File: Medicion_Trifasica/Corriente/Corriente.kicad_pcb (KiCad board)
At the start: 4 copper layers, 49 x 25 mm, 13 parts, among them IC1 AMS1117-3.3, J1 XADC_Input, J2 Screw_Terminal_01x02, J3 XADC_Ref, J4 XADC_Input, U1 ACS725xLCTR-20AB, U2 LM358

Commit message: PCB de la medicion de corriente
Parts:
- moved C3 76.8 mm to (155.4, 97.2)
- moved J1 76.8 mm to (167.8, 103.0)
- moved J2 76.8 mm to (129.5, 103.4)
- moved J3 76.8 mm to (167.8, 99.4)
- moved J4 76.8 mm to (151.9, 89.3)
- moved R1 76.8 mm to (145.4, 105.3)
- moved R2 76.8 mm to (146.4, 108.3)
- moved R3 76.8 mm to (160.3, 95.7)
- moved U1 76.8 mm to (137.4, 105.9)
- moved U2 76.8 mm to (152.8, 104.6)
- moved C1 76.8 mm to (141.7, 107.4)
- moved IC1 76.8 mm to (149.4, 96.1)
- moved R4 76.8 mm to (163.7, 96.6)

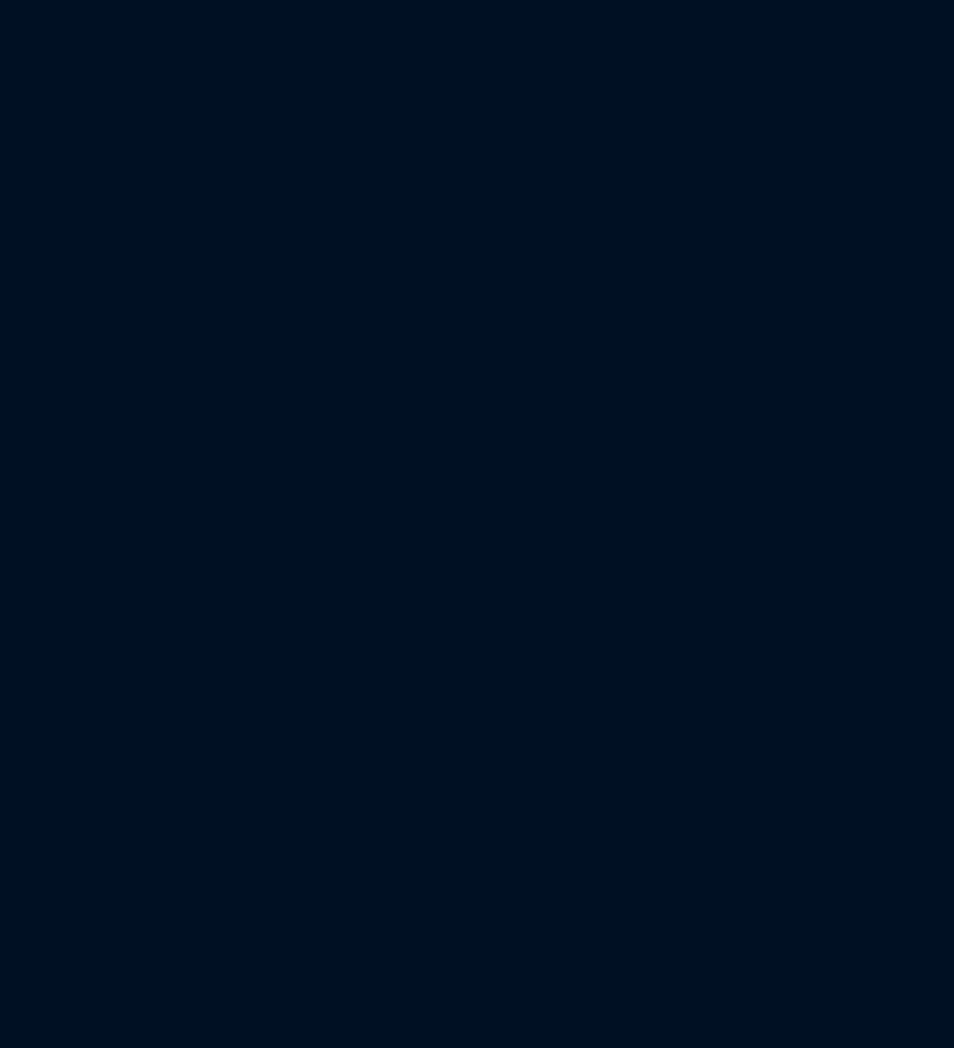
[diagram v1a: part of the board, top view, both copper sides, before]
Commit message: Correciones PCBs
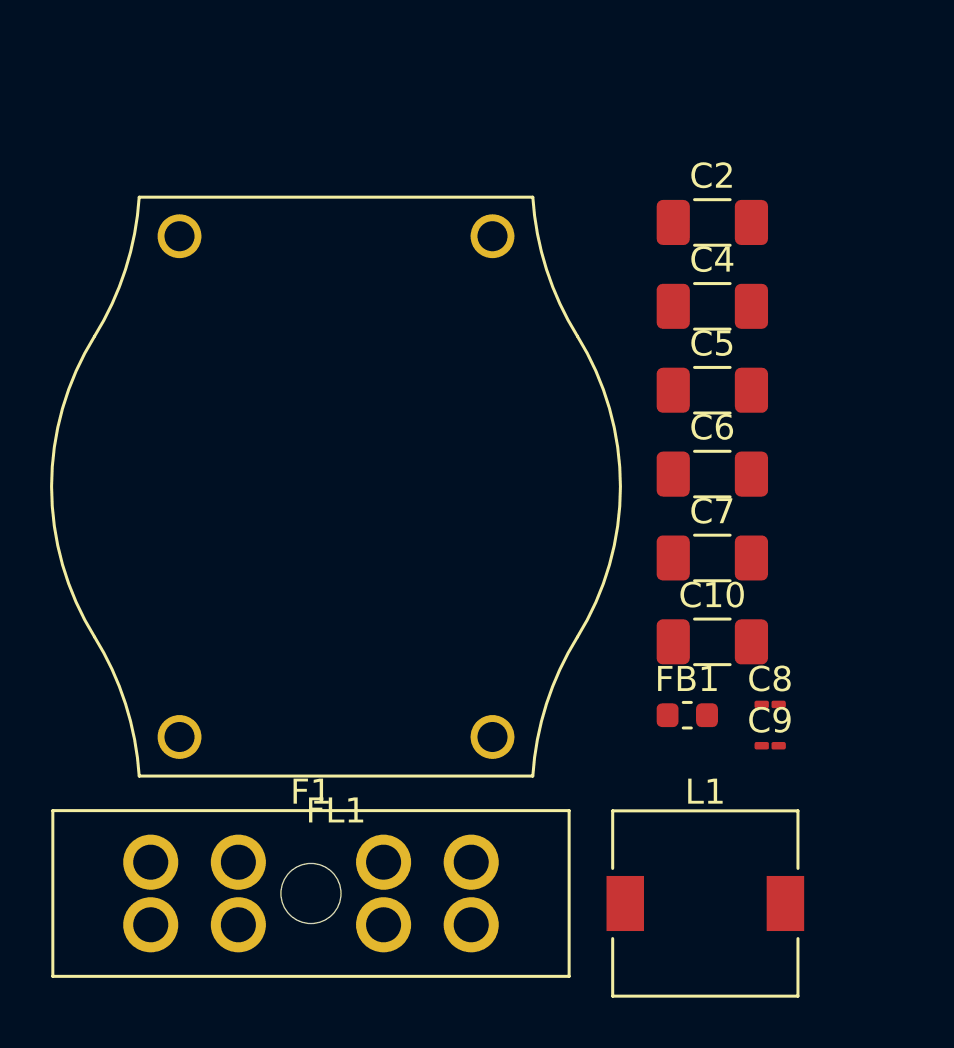
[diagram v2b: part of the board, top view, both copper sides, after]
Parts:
- added C10: 100 nF, Capacitor_SMD:C_1206_3216Metric_Pad1.33x1.80mm_HandSolder, F.Cu at (105.0, 115.7)
- added C2: 0.1 uF, Capacitor_SMD:C_1206_3216Metric_Pad1.33x1.80mm_HandSolder, F.Cu at (105.0, 98.9)
- added C4: 470 uF, Capacitor_SMD:C_1206_3216Metric_Pad1.33x1.80mm_HandSolder, F.Cu at (105.0, 102.2)
- added C5: 100 nF, Capacitor_SMD:C_1206_3216Metric_Pad1.33x1.80mm_HandSolder, F.Cu at (105.0, 105.6)
- added C6: 100 nF, Capacitor_SMD:C_1206_3216Metric_Pad1.33x1.80mm_HandSolder, F.Cu at (105.0, 109.0)
- added C7: 100 nF, Capacitor_SMD:C_1206_3216Metric_Pad1.33x1.80mm_HandSolder, F.Cu at (105.0, 112.3)
- added C8: 100pF, Capacitor_SMD:C_01005_0402Metric_Pad0.57x0.30mm_HandSolder, F.Cu at (107.3, 118.2)
- added C9: 4.7 nF, Capacitor_SMD:C_01005_0402Metric_Pad0.57x0.30mm_HandSolder, F.Cu at (107.3, 119.8)
- added F1: Fuse, Fuse:FuseHolder_Blade_ATO_Littelfuse_FLR_178.6165, F.Cu at (82.5, 124.5)
- added FB1: FerriteBead_Small, Inductor_SMD:L_0603_1608Metric, F.Cu at (104.0, 118.6)
- added FL1: Choke_CommonMode_FerriteCore_1234, Inductor_THT:Choke_EPCOS_B82722A, F.Cu at (83.7, 119.5)
- added L1: L, Inductor_SMD:L_7.3x7.3_H3.5, F.Cu at (104.7, 126.1)
- J4: value XADC_Input -> POWER
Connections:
- J4 pad 1: +9V -> Net-(J4-Pin_1)
- J4 pad 2: GND -> Net-(J4-Pin_2)
- R3 pad 1: +3V3 -> Net-(FB1-Pad2)
- U1 pad 1: Net-(J2-Pin_1) -> Net-(F1-Pad2)
- U1 pad 2: Net-(J2-Pin_1) -> Net-(F1-Pad2)

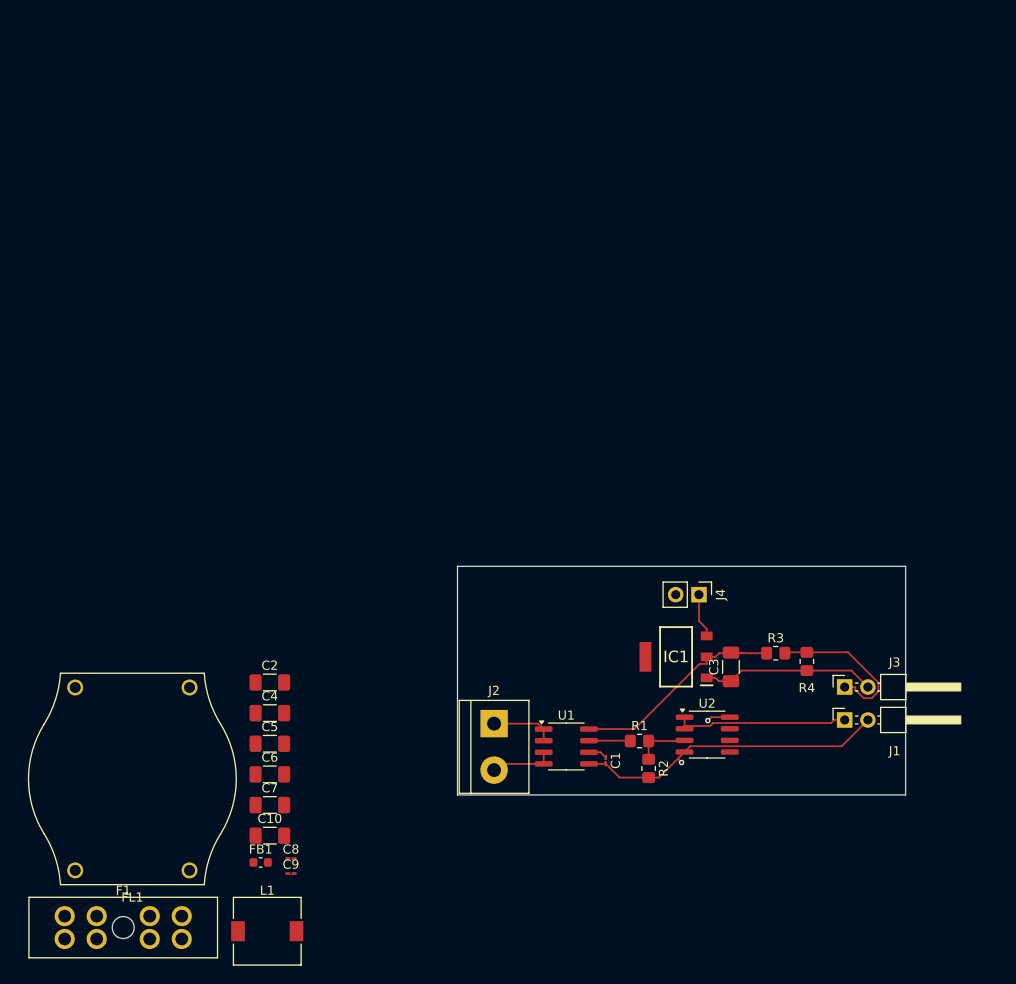
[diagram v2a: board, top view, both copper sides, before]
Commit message: Mejora en la organizacion de los circuitos con netclases y colores
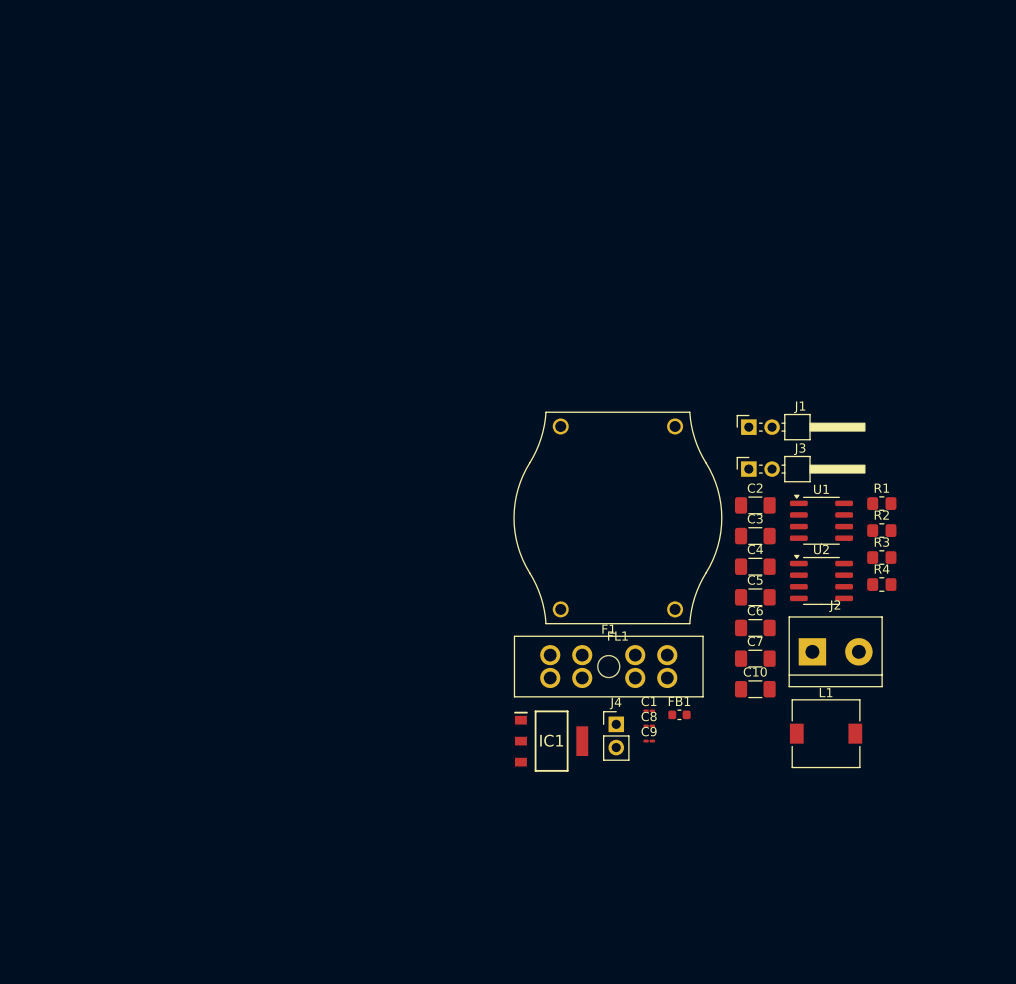
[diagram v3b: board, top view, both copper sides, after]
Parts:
- moved L1 64.8 mm to (165.8, 104.5)
- moved F1 60.3 mm to (135.6, 95.9)
- moved FL1 60.3 mm to (136.8, 90.9)
- moved C2 56.5 mm to (158.1, 79.5)
- moved C10 55.5 mm to (158.1, 99.6)
- moved C4 55.5 mm to (158.1, 86.2)
- moved C5 55.5 mm to (158.1, 89.6)
- moved C6 55.5 mm to (158.1, 92.9)
- moved C7 55.5 mm to (158.1, 96.3)
- moved FB1 48.6 mm to (149.8, 102.4)
- moved C8 41.8 mm to (146.5, 103.7)
- moved C9 41.8 mm to (146.5, 105.3)
- moved U1 37.2 mm to (165.3, 81.2)
- moved R1 37.1 mm to (171.9, 79.3)
- moved R2 36.4 mm to (171.9, 82.3), turned to 0 degrees
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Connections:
- net Net-(F1-Pad2) renamed /IP+
- net Net-(J1-Pin_1) renamed /XADC_Input
- net Net-(J2-Pin_1) renamed /CURRENT_FUSE
- net Net-(J2-Pin_2) renamed /IP-
- net Net-(J3-Pin_1) renamed /XADC_VREF
- net Net-(U1-FILTER) renamed /FILTER_CS
- net Net-(U1-VIOUT) renamed /V_SENSOR_OUT
- net Net-(U2A-+) renamed /V_SENSOR_DIV
- C4 pad 1: Net-(J4-Pin_2) -> /INPUT_+9V
- C4 pad 2: Net-(J4-Pin_1) -> /INPUT_GND
- FL1 pad 1: Net-(J4-Pin_2) -> /INPUT_+9V
- FL1 pad 3: Net-(J4-Pin_1) -> /INPUT_GND
- J4 pad 1: Net-(J4-Pin_1) -> /INPUT_+9V
- J4 pad 2: Net-(J4-Pin_2) -> /INPUT_GND
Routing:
- net GND: track 77.5 -> 0.00 mm, vias 1 -> 0
- net +3V3: track 24.8 -> 0.00 mm
- net +9V: track 21.6 -> 0.00 mm, vias 1 -> 0
- net /XADC_Input: track 19.1 -> 0.00 mm
- net /XADC_VREF: track 17.3 -> 0.00 mm
- net /IP-: track 6.97 -> 0.00 mm
- net /CURRENT_FUSE: track 6.94 -> 0.00 mm
- net /V_SENSOR_DIV: track 5.95 -> 0.00 mm
- net /V_SENSOR_OUT: track 4.54 -> 0.00 mm
- net /FILTER_CS: track 2.06 -> 0.00 mm
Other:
- board outline removed

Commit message: Mejoras y trabajos realizadps
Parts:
- removed FL1: Choke_CommonMode_FerriteCore_1234, Inductor_THT:Choke_EPCOS_B82722A
- C1, C8, C9: footprint Capacitor_SMD:C_01005_0402Metric_Pad0.57x0.30mm_HandSolder -> Capacitor_SMD:C_1206_3216Metric_Pad1.33x1.80mm_HandSolder
- moved J2 52.3 mm to (112.1, 98.5), turned to -90 degrees
- moved L1 38.5 mm to (135.2, 81.1)
- moved C4 31.9 mm to (126.4, 82.7), turned to -90 degrees
- moved J4 29.9 mm to (123.0, 81.1)
- moved C5 29.2 mm to (129.7, 82.7), turned to 90 degrees
- moved U1 25.4 mm to (150.3, 101.7)
- moved IC1 25.1 mm to (148.5, 83.7), turned to -90 degrees
- moved R1 24.2 mm to (160.7, 100.8)
- moved J1 22.0 mm to (171.8, 87.5)
- moved J3 21.2 mm to (171.9, 91.1)
- moved C6 20.0 mm to (144.6, 78.1)
- moved C8 19.1 mm to (163.2, 94.5), turned to 180 degrees
- moved FB1 18.3 mm to (167.4, 97.4)
- moved C2 17.4 mm to (140.7, 79.6), turned to -90 degrees
- moved R2 13.2 mm to (162.7, 91.8)
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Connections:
- C4 pad 2: /INPUT_GND -> GND
- C5 pad 2: Net-(C5-Pad2) -> /INPUT_+9V
- J4 pad 2: /INPUT_GND -> GND
- L1 pad 1: Net-(C5-Pad2) -> /INPUT_+9V
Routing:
- net +3V3: track 0.00 -> 46.6 mm, vias 0 -> 3
- net /IP-: track 0.00 -> 38.6 mm
- net GND: track 0.00 -> 31.4 mm, vias 0 -> 21
- net /IP+: track 0.00 -> 25.9 mm
- net /CURRENT_FUSE: track 0.00 -> 24.4 mm
- net +9V: track 0.00 -> 24.2 mm
- net /V_SENSOR_DIV: track 0.00 -> 19.6 mm, vias 0 -> 2
- net /XADC_Input: track 0.00 -> 12.0 mm
- net /XADC_VREF: track 0.00 -> 10.7 mm
- net /INPUT_+9V: track 0.00 -> 8.97 mm
- net /V_SENSOR_OUT: track 0.00 -> 6.99 mm
- net /FILTER_CS: track 0.00 -> 2.57 mm
- net Net-(FB1-Pad2): track 0.00 -> 1.71 mm
- added copper zone on In1.Cu, net GND
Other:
- board outline added: 70 x 35 mm
